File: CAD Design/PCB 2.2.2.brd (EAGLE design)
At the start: 70 x 44.9 mm, 46 parts, among them U1 CC2538, U2 MAX1555, X1 32MHz, X2 FC-12M

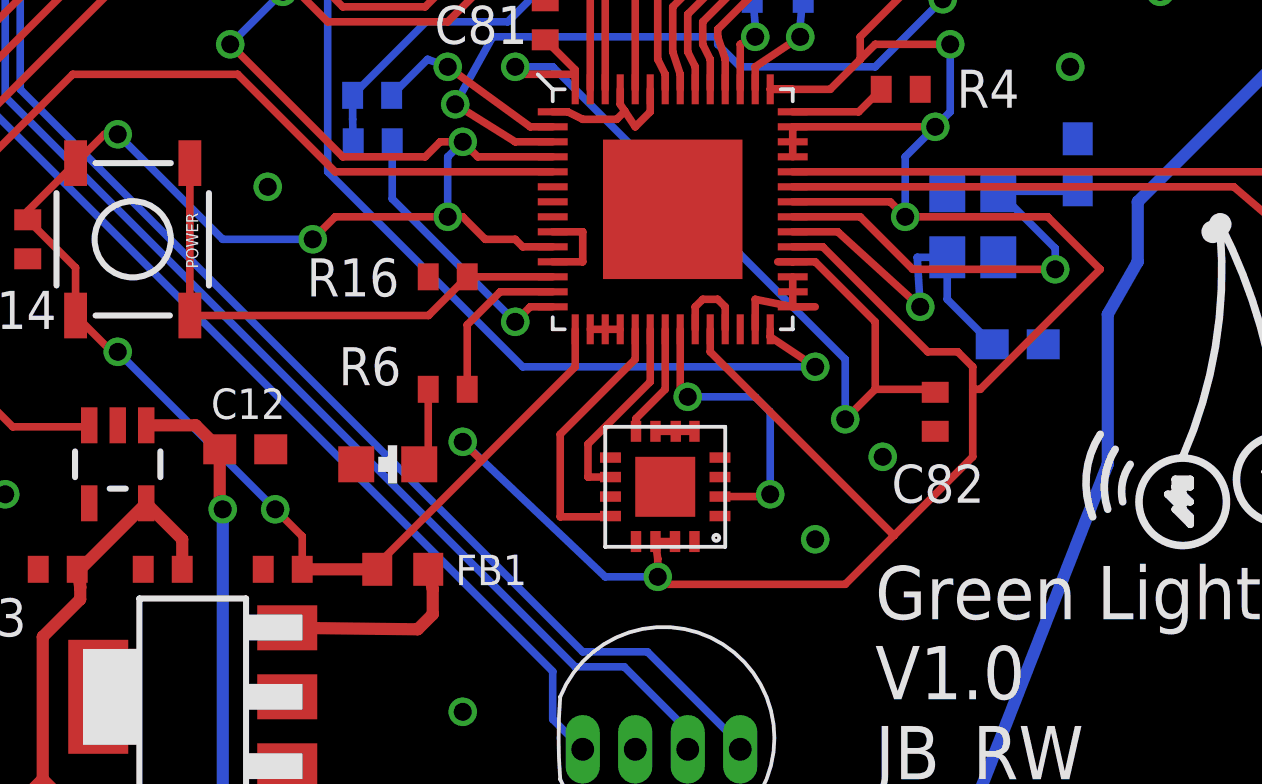
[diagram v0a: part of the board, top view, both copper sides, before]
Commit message: Version Update - 2.5
Cleaned up Schematic for part placement reference.  SW1 to be modified.
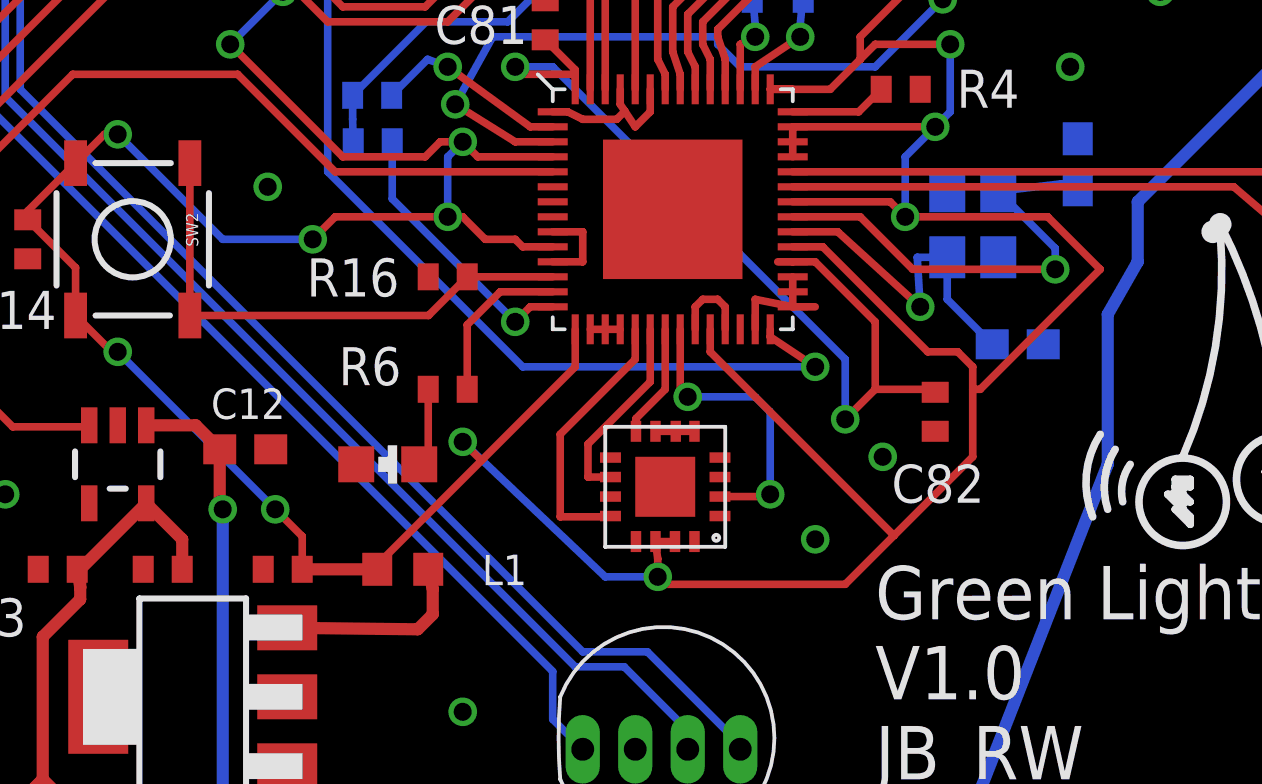
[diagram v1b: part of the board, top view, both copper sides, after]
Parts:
- C5: value 1n -> 0.1u
- R17: value 478 -> 442
- renumbered FB1 to L1, POWER to SW2
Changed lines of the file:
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@@
 <grid distance="0.25" unitdist="mm" unit="mm" style="lines" multiple="1" display="yes" altdistance="0.125" altunitdist="mm" altunit="mm"/>
 <layers>
-<layer number="1" name="Top" color="4" fill="1" visible="yes" active="yes"/>
+<layer number="1" name="Top" color="4" fill="1" visible="no" active="yes"/>
 <layer number="16" name="Bottom" color="1" fill="1" visible="yes" active="yes"/>
 <layer number="17" name="Pads" color="2" fill="1" visible="yes" active="yes"/>
@@
 </autorouter>
 <elements>
-<element name="FB1" library="discrete" package="R603" value="" x="25" y="9.5" smashed="yes" rot="R180">
+<element name="L1" library="discrete" package="R603" value="" x="25" y="9.5" smashed="yes" rot="R180">
 <attribute name="NAME" x="29.139" y="9.988" size="1.016" layer="25" rot="R180"/>
 <attribute name="VALUE" x="25.889" y="11.532" size="1.016" layer="27" rot="R180"/>
@@
 <attribute name="VALUE" x="27.135" y="21.155" size="1.27" layer="27" rot="R180"/>
 </element>
-<element name="POWER" library="SparkFun-Electromechanical" package="TACTILE_SWITCH_SMD" value="" x="16" y="20.5" smashed="yes" rot="R270">
+<element name="SW2" library="SparkFun-Electromechanical" package="TACTILE_SWITCH_SMD" value="" x="16" y="20.5" smashed="yes" rot="R270">
 <attribute name="PROD_ID" value="SWCH-08247" x="-13.21" y="3.99" size="1.778" layer="27" rot="R270" display="off"/>
 <attribute name="NAME" x="17.778" y="21.389" size="0.4064" layer="25" rot="R270"/>
@@
 <attribute name="VALUE" x="17.635" y="11.405" size="1.27" layer="27" rot="R180"/>
 </element>
-<element name="C5" library="discrete" package="C0402" value="1n" x="22" y="42" smashed="yes" rot="R180">
+<element name="C5" library="discrete" package="C0402" value="0.1u" x="22" y="42" smashed="yes" rot="R180">
 <attribute name="NAME" x="20.385" y="41.238" size="1.27" layer="25" rot="R180"/>
 </element>
@@
 <attribute name="VALUE" x="13.0888" y="36.3328" size="1.016" layer="27" ratio="10" rot="R270"/>
 </element>
-<element name="R17" library="rcl" package="R0402" value="478" x="26" y="37" smashed="yes">
+<element name="R17" library="rcl" package="R0402" value="442" x="26" y="37" smashed="yes">
 <attribute name="NAME" x="27.615" y="36.135" size="1.27" layer="25"/>
 <attribute name="VALUE" x="25.365" y="35.095" size="1.27" layer="27"/>
@@
 <contactref element="U1" pad="4"/>
 <contactref element="U1" pad="43"/>
-<contactref element="FB1" pad="2"/>
+<contactref element="L1" pad="2"/>
 <contactref element="JTAG" pad="1"/>
 <contactref element="JTAG" pad="2"/>
-<contactref element="POWER" pad="3"/>
-<contactref element="POWER" pad="4"/>
+<contactref element="SW2" pad="3"/>
+<contactref element="SW2" pad="4"/>
 <contactref element="C3" pad="2"/>
 <wire x1="24.15" y1="9.5" x2="21.65" y2="9.5" width="0.4064" layer="1"/>
@@
 </signal>
 <signal name="N$17">
-<contactref element="FB1" pad="1"/>
+<contactref element="L1" pad="1"/>
 <contactref element="VREG1" pad="3"/>
 <wire x1="21.15" y1="7.55" x2="25.5" y2="7.5" width="0.4064" layer="1"/>
@@
 <contactref element="X1" pad="3"/>
 <contactref element="C8" pad="2"/>
-<wire x1="47.5" y1="22.15" x2="47.45" y2="22.1" width="0.254" layer="16"/>
-<wire x1="47.45" y1="22.1" x2="44.85" y2="22.1" width="0.254" layer="16"/>
+<wire x1="47.5" y1="22.15" x2="46.95" y2="22.35" width="0.254" layer="16"/>
+<wire x1="46.95" y1="22.35" x2="44.85" y2="22.1" width="0.254" layer="16"/>
 <wire x1="44.85" y1="22.1" x2="46.75" y2="20.2" width="0.254" layer="16"/>
 <wire x1="46.75" y1="20.2" x2="46.75" y2="19.5" width="0.254" layer="16"/>
@@
 <signal name="N$3">
 <contactref element="U1" pad="12"/>
-<contactref element="POWER" pad="1"/>
-<contactref element="POWER" pad="2"/>
+<contactref element="SW2" pad="1"/>
+<contactref element="SW2" pad="2"/>
 <contactref element="R16" pad="1"/>
 <wire x1="17.905" y1="23.04" x2="17.905" y2="17.96" width="0.254" layer="1"/>
